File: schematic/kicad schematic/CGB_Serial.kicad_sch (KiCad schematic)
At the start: 10 parts, among them P3 Conn_01x06

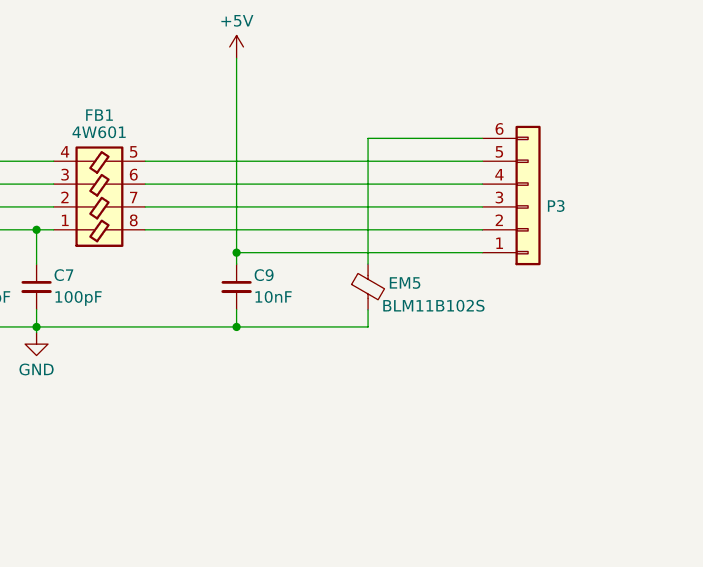
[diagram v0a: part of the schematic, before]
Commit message: fixed schematic, thx giltesa and darren
the ir transistor was labelled wrong
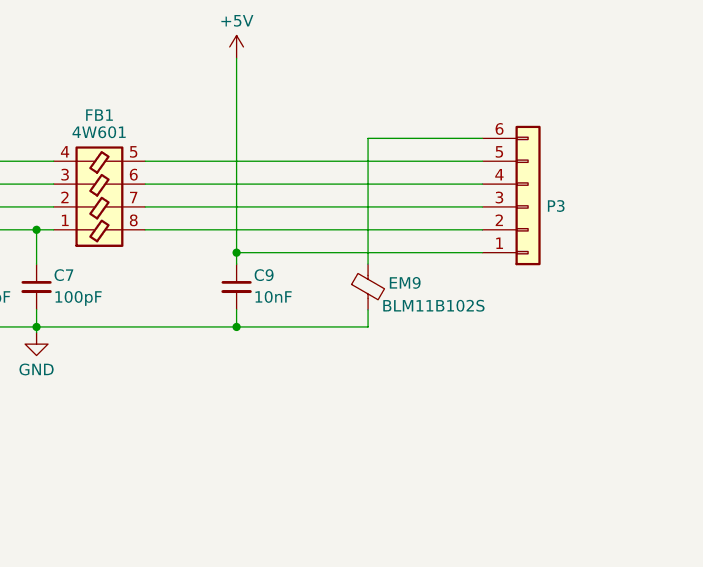
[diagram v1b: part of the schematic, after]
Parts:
- renumbered EM5 to EM9
